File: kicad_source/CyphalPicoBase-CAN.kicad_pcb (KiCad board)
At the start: 2 copper layers, 52 x 36 mm, 62 parts, among them CN1 RASPBERRYPI_PICO, CN12 S3B-PH-SM4-TB, CN2 SM04B-SRSS-TB, CN3 SM04B-SRSS-TB, CN4 SM04B-GHS-TB, CN5 SM04B-GHS-TB, CN7 DNI, CN8 DNI, SW1 PTS636 SM43 SMTR LFS, U3 M24C64-RMN6TP, U8 MCP2515T-I/SO, U9 SN65HVD230, Y1 X322516MLB4SI

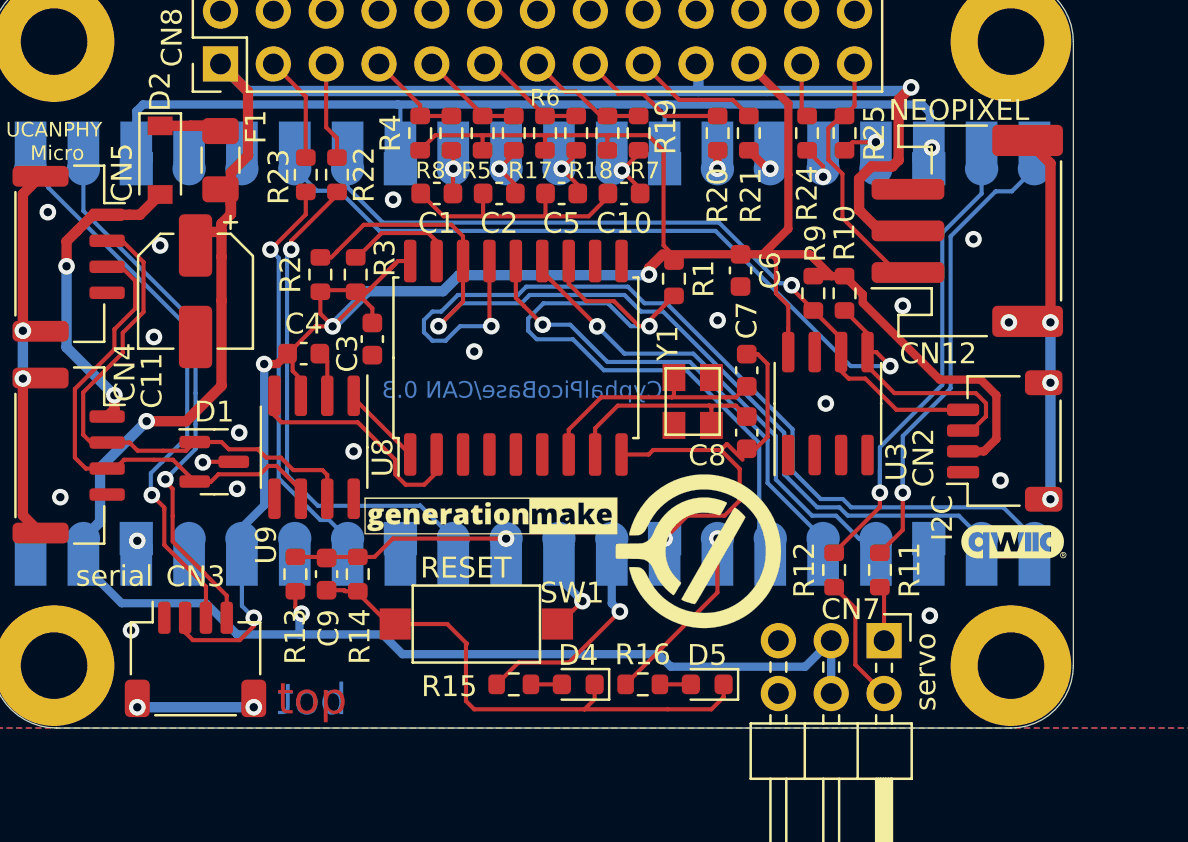
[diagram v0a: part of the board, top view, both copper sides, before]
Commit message: updated step file of PCB, added JST conectors
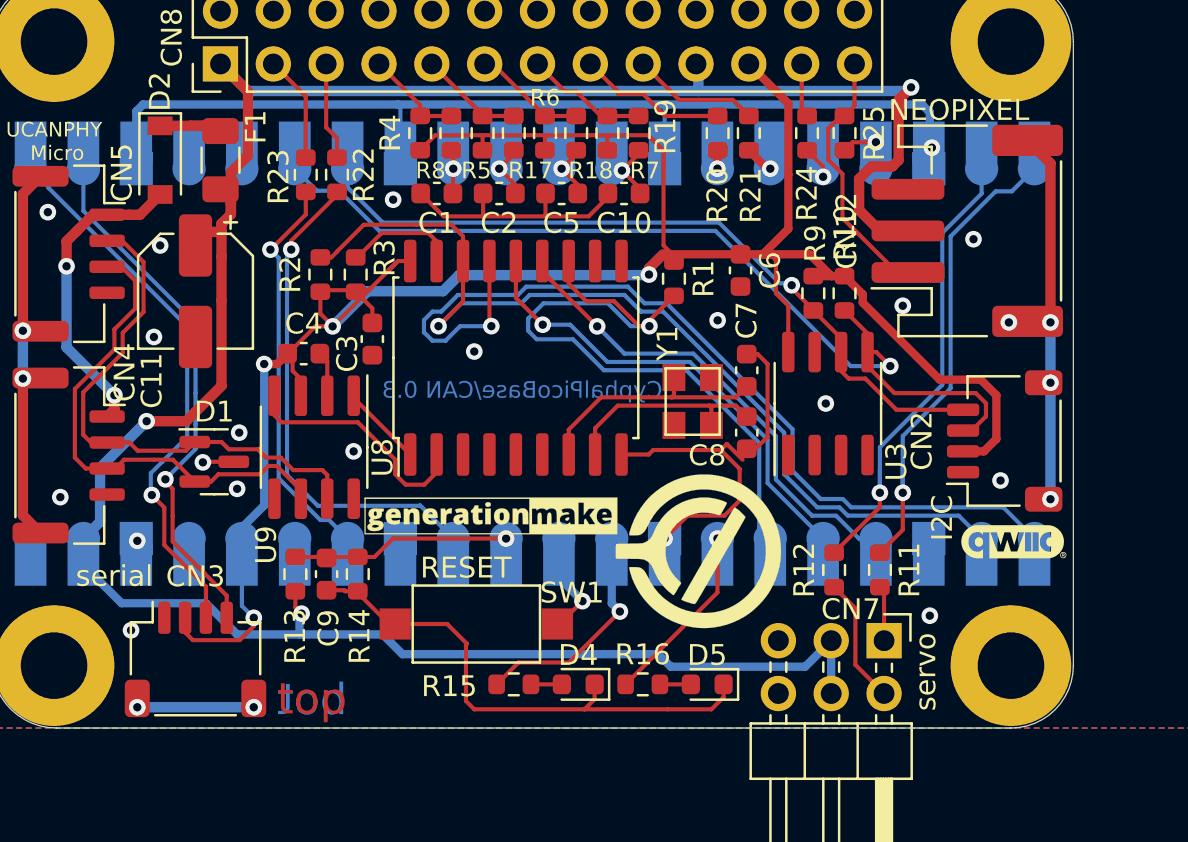
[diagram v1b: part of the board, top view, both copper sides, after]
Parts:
- CN12: footprint Connector_JST:JST_PH_S3B-PH-SM4-TB_1x03-1MP_P2.00mm_Horizontal -> generationmake:JST_PH_S3B-PH-SM4-TB_1x03-1MP_P2.00mm_Horizontal
- CN2, CN3: footprint Connector_JST:JST_SH_SM04B-SRSS-TB_1x04-1MP_P1.00mm_Horizontal -> generationmake:JST_SH_SM04B-SRSS-TB_1x04-1MP_P1.00mm_Horizontal
